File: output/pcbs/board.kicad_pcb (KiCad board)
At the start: 2 copper layers, 134.2 x 121.1 mm, 59 parts

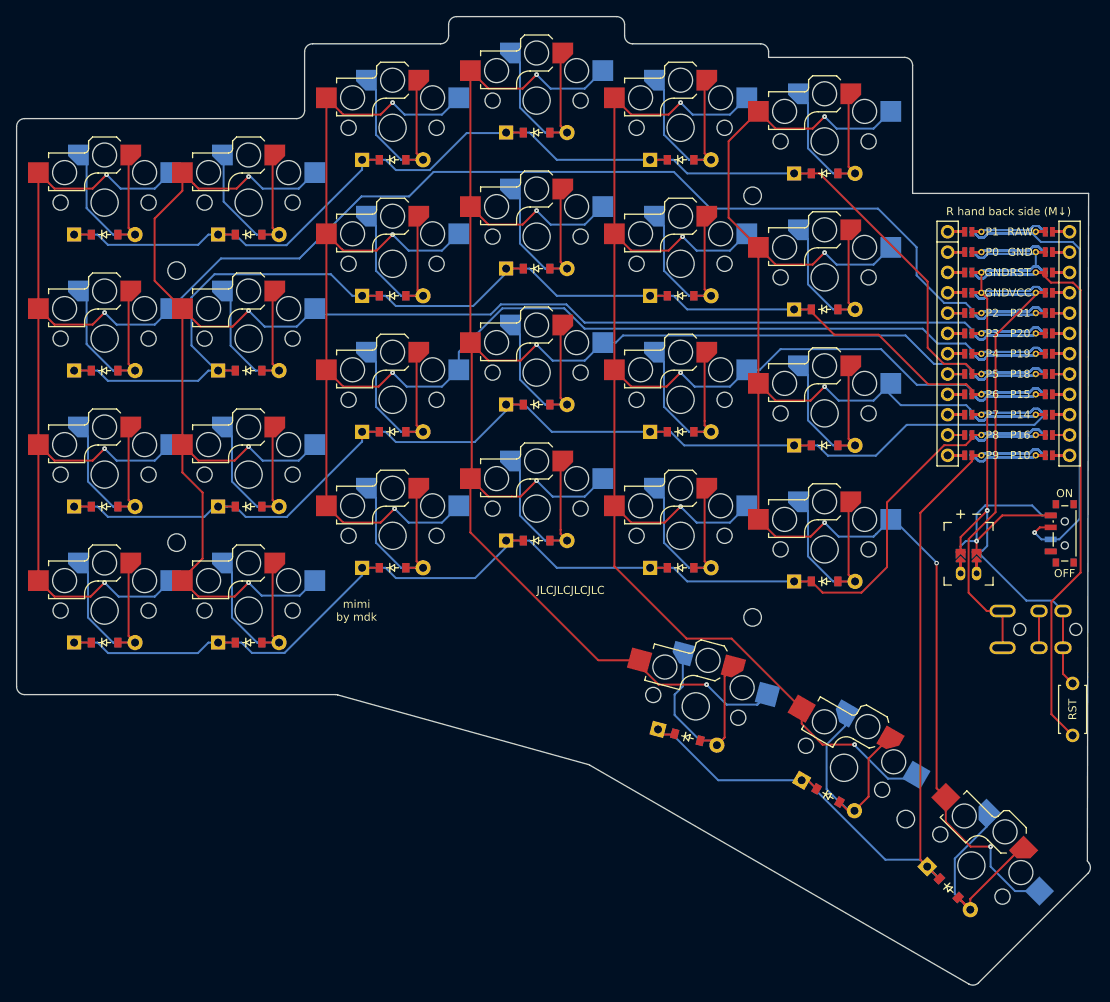
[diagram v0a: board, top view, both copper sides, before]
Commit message: fix trrs routing
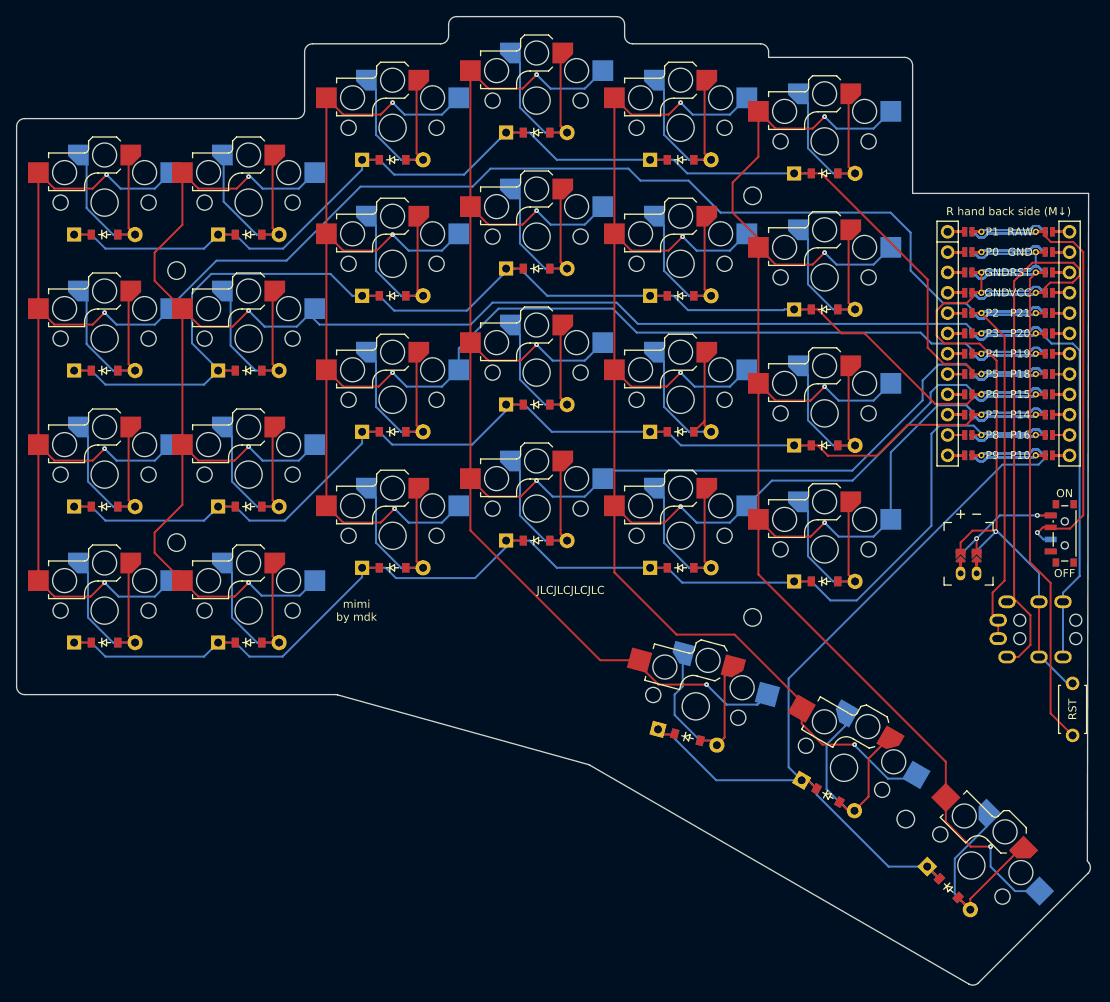
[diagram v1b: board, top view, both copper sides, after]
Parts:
- TRRS1: footprint ceoloide:trrs_pj320a (reversible, symmetric) -> ceoloide:trrs_pj320a (reversible)
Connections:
- TRRS1 pad 2: GND -> P3
- TRRS1 pad 3: DAT -> GND
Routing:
- net P3: track 58.2 -> 112.7 mm
- net P2: track 58.2 -> 111.2 mm
- net GND: track 242.3 -> 280.4 mm
- net P14: track 261.9 -> 288.8 mm, vias 6 -> 5
- net VCC: track 109.0 -> 134.6 mm
- net P18: track 293.8 -> 309.8 mm
- net P8: track 209.8 -> 224.9 mm
- net P15: track 278.8 -> 293.0 mm
- net P9: track 163.9 -> 176.8 mm
- net BAT_P: track 28.3 -> 16.3 mm, vias 1 -> 2
- net P6: track 214.0 -> 225.8 mm
- net P5: track 210.8 -> 221.7 mm
- net P21: track 304.2 -> 315.1 mm
- net P20: track 279.6 -> 289.6 mm
- net P19: track 259.4 -> 269.2 mm
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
